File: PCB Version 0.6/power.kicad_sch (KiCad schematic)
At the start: 32 parts, among them IC5 LMR38025SDRRR, IC6 LMR38025SDRRR, U2 C5250982, U4 TPS2116DRL, U7 TPS746-3.3DRV

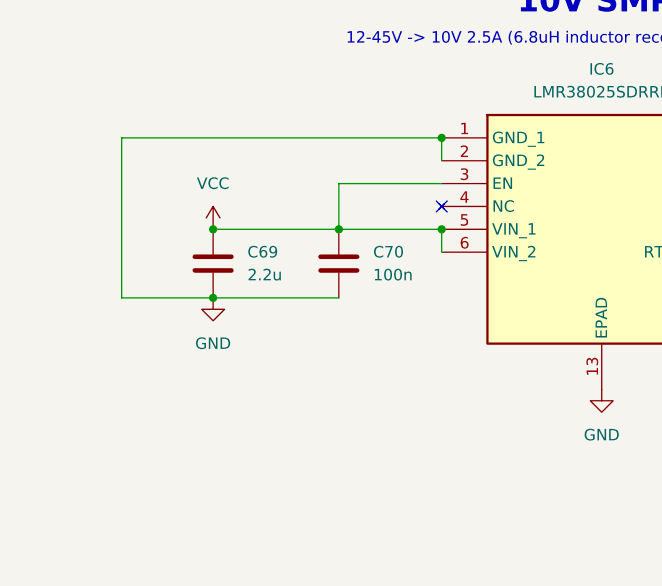
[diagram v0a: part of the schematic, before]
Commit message: remove current sensor ADC, swap opamp, add dcdc switch
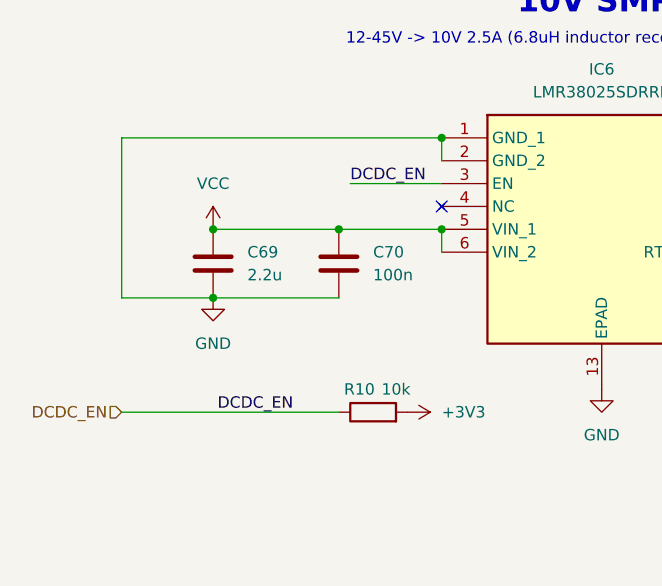
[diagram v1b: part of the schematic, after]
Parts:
- added R10: 10k, Resistor_SMD:R_0402_1005Metric, symbol Device:R
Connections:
- net VCC: no longer IC6.3 (EN)
- new net +3V3: R10.2
- new net DCDC_EN: IC6.3 (EN), R10.1
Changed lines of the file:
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@@
+	(wire
+		(pts
+			(xy 53.34 118.11) (xy 63.5 118.11)
+		)
+		(stroke
+			(width 0)
+			(type default)
+		)
+	)
 	(wire
 		(pts
@@
 	(wire
 		(pts
-			(xy 52.07 118.11) (xy 52.07 123.19)
-		)
-		(stroke
-			(width 0)
-			(type default)
-		)
-	)
-	(wire
-		(pts
 			(xy 265.43 123.19) (xy 265.43 121.92)
 		)
@@
 	(wire
 		(pts
+			(xy 27.94 143.51) (xy 52.07 143.51)
+		)
+		(stroke
+			(width 0)
+			(type default)
+		)
+	)
+	(wire
+		(pts
 			(xy 229.87 121.92) (xy 240.03 121.92)
 		)
@@
 	(wire
 		(pts
-			(xy 63.5 118.11) (xy 52.07 118.11)
-		)
-		(stroke
-			(width 0)
-			(type default)
-		)
-	)
-	(wire
-		(pts
 			(xy 109.22 113.03) (xy 113.03 113.03)
 		)
@@
 			(width 0)
 			(type default)
+		)
+	)
+	(label "DCDC_EN"
+		(at 53.34 118.11 0)
+		(effects
+			(font
+				(size 1.27 1.27)
+			)
+			(justify left bottom)
+		)
+	)
+	(label "DCDC_EN"
+		(at 46.99 143.51 180)
+		(effects
+			(font
+				(size 1.27 1.27)
+			)
+			(justify right bottom)
+		)
+	)
+	(hierarchical_label "DCDC_EN"
+		(shape input)
+		(at 27.94 143.51 180)
+		(effects
+			(font
+				(size 1.27 1.27)
+			)
+			(justify right)
 		)
 	)
@@
 	)
 	(symbol
+		(lib_id "Device:R")
+		(at 55.88 143.51 90)
+		(unit 1)
+		(exclude_from_sim no)
+		(in_bom yes)
+		(on_board yes)
+		(dnp no)
+		(property "Reference" "R10"
+			(at 54.356 140.97 90)
+			(effects
+				(font
+					(size 1.27 1.27)
+				)
+			)
+		)
+		(property "Value" "10k"
+			(at 58.42 140.97 90)
+			(effects
+				(font
+					(size 1.27 1.27)
+				)
+			)
+		)
+		(property "Footprint" "Resistor_SMD:R_0402_1005Metric"
+			(at 55.88 145.288 90)
+			(effects
+				(font
+					(size 1.27 1.27)
+				)
+				(hide yes)
+			)
+		)
+		(property "Datasheet" "~"
+			(at 55.88 143.51 0)
+			(effects
+				(font
+					(size 1.27 1.27)
+				)
+				(hide yes)
+			)
+		)
+		(property "Description" "Resistor"
+			(at 55.88 143.51 0)
+			(effects
+				(font
+					(size 1.27 1.27)
+				)
+				(hide yes)
+			)
+		)
+		(pin "2"
+		)
+		(pin "1"
+		)
+		(instances
+			(project ""
+				(path "/1651f454-30c0-48ea-9fcf-6c96a661786a/c47ad1ff-c88e-42df-ba75-e03e62e860dd"
+					(reference "R10")
+					(unit 1)
+				)
+			)
+		)
+	)
+	(symbol
 		(lib_id "power:GND")
 		(at 127 71.12 0)
@@
 					(unit 1)
 				)
+			)
+		)
+	)
+	(symbol
+		(lib_id "power:+3V3")
+		(at 59.69 143.51 270)
+		(unit 1)
+		(exclude_from_sim no)
+		(in_bom yes)
+		(on_board yes)
+		(dnp no)
+		(fields_autoplaced yes)
+		(property "Reference" "#PWR030"
+			(at 55.88 143.51 0)
+			(effects
+				(font
+					(size 1.27 1.27)
+				)
+				(hide yes)
+			)
+		)
+		(property "Value" "+3V3"
+			(at 63.5 143.5099 90)
+			(effects
+				(font
+					(size 1.27 1.27)
+				)
+				(justify left)
+			)
+		)
+		(property "Footprint" ""
+			(at 59.69 143.51 0)
+			(effects
+				(font
+					(size 1.27 1.27)
+				)
+				(hide yes)
+			)
+		)
+		(property "Datasheet" ""
+			(at 59.69 143.51 0)
+			(effects
+				(font
+					(size 1.27 1.27)
+				)
+				(hide yes)
+			)
+		)
+		(property "Description" "Power symbol creates a global label with name \"+3V3\""
+			(at 59.69 143.51 0)
+			(effects
+				(font
+					(size 1.27 1.27)
+				)
+				(hide yes)
+			)
+		)
+		(pin "1"
+		)
+		(instances
+			(project ""
+				(path "/1651f454-30c0-48ea-9fcf-6c96a661786a/c47ad1ff-c88e-42df-ba75-e03e62e860dd"
+					(reference "#PWR030")
+					(unit 1)
+				)

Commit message: Update power.kicad_sch
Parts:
- added C31: 10u, Capacitor_SMD:C_0402_1005Metric, symbol Device:C
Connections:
- net +3V3_ELRS: now also C31.1
- net GND: now also C31.2
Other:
- moved on the sheet: C83, C84, U7

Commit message: WIP layout
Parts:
- C65, C70, C71, C84: footprint Capacitor_SMD:C_0402_1005Metric_Pad0.74x0.62mm_HandSolder -> Capacitor_SMD:C_0402_1005Metric
- R13, R14, R15, R16, R17, R18, R19, R20: footprint Resistor_SMD:R_0402_1005Metric_Pad0.72x0.64mm_HandSolder -> Resistor_SMD:R_0402_1005Metric
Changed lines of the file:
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@@
 			)
 		)
-		(property "Footprint" "Resistor_SMD:R_0402_1005Metric_Pad0.72x0.64mm_HandSolder"
+		(property "Footprint" "Resistor_SMD:R_0402_1005Metric"
 			(at 186.182 63.5 90)
 			(effects
@@
 			)
 		)
-		(property "Footprint" "Resistor_SMD:R_0402_1005Metric_Pad0.72x0.64mm_HandSolder"
+		(property "Footprint" "Resistor_SMD:R_0402_1005Metric"
 			(at 114.3 72.898 90)
 			(effects
@@
 			)
 		)
-		(property "Footprint" "Resistor_SMD:R_0402_1005Metric_Pad0.72x0.64mm_HandSolder"
+		(property "Footprint" "Resistor_SMD:R_0402_1005Metric"
 			(at 114.3 135.128 90)
 			(effects
@@
 			)
 		)
-		(property "Footprint" "Resistor_SMD:R_0402_1005Metric_Pad0.72x0.64mm_HandSolder"
+		(property "Footprint" "Resistor_SMD:R_0402_1005Metric"
 			(at 125.222 118.11 90)
 			(effects
@@
 			)
 		)
-		(property "Footprint" "Resistor_SMD:R_0402_1005Metric_Pad0.72x0.64mm_HandSolder"
+		(property "Footprint" "Resistor_SMD:R_0402_1005Metric"
 			(at 125.222 128.27 90)
 			(effects
@@
 			)
 		)
-		(property "Footprint" "Capacitor_SMD:C_0402_1005Metric_Pad0.74x0.62mm_HandSolder"
+		(property "Footprint" "Capacitor_SMD:C_0402_1005Metric"
 			(at 108.2548 113.03 0)
 			(effects
@@
 			)
 		)
-		(property "Footprint" "Capacitor_SMD:C_0402_1005Metric_Pad0.74x0.62mm_HandSolder"
+		(property "Footprint" "Capacitor_SMD:C_0402_1005Metric"
 			(at 263.8552 130.81 0)
 			(effects
@@
 			)
 		)
-		(property "Footprint" "Capacitor_SMD:C_0402_1005Metric_Pad0.74x0.62mm_HandSolder"
+		(property "Footprint" "Capacitor_SMD:C_0402_1005Metric"
 			(at 108.2548 50.8 0)
 			(effects
@@
 			)
 		)
-		(property "Footprint" "Capacitor_SMD:C_0402_1005Metric_Pad0.74x0.62mm_HandSolder"
+		(property "Footprint" "Capacitor_SMD:C_0402_1005Metric"
 			(at 53.0352 130.81 0)
 			(effects
@@
 			)
 		)
-		(property "Footprint" "Resistor_SMD:R_0402_1005Metric_Pad0.72x0.64mm_HandSolder"
+		(property "Footprint" "Resistor_SMD:R_0402_1005Metric"
 			(at 125.222 66.04 90)
 			(effects
@@
 			)
 		)
-		(property "Footprint" "Resistor_SMD:R_0402_1005Metric_Pad0.72x0.64mm_HandSolder"
+		(property "Footprint" "Resistor_SMD:R_0402_1005Metric"
 			(at 125.222 55.88 90)
 			(effects
@@
 			)
 		)
-		(property "Footprint" "Resistor_SMD:R_0402_1005Metric_Pad0.72x0.64mm_HandSolder"
+		(property "Footprint" "Resistor_SMD:R_0402_1005Metric"
 			(at 186.182 71.12 90)
 			(effects

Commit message: wip layout
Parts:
- removed C82: 1u, Capacitor_SMD:C_0402_1005Metric, symbol Device:C
- C63, C64: footprint Capacitor_SMD:C_0603_1608Metric -> Capacitor_SMD:C_0402_1005Metric
- C68, C69: value 2.2u -> 4.7u; footprint Capacitor_SMD:C_1206_3216Metric -> Capacitor_SMD:C_0805_2012Metric
- U7: footprint Package_SON:WSON-6-1EP_2x2mm_P0.65mm_EP1x1.6mm_ThermalVias -> Package_SON:WSON-6-1EP_2x2mm_P0.65mm_EP1x1.6mm
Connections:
- net +3V3_ELRS is gone; now on net +3V3: C31.1, C84.1, U7.1 (OUT)
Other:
- moved on the sheet: C88
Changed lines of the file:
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@@
 	)
 	(junction
-		(at 195.58 128.27)
-		(diameter 0)
-		(color 0 0 0 0)
-	)
-	(junction
 		(at 274.32 121.92)
 		(diameter 0)
@@
 	)
 	(junction
-		(at 207.01 120.65)
-		(diameter 0)
-		(color 0 0 0 0)
-	)
-	(junction
 		(at 63.5 50.8)
 		(diameter 0)
@@
 	)
 	(junction
-		(at 195.58 120.65)
-		(diameter 0)
-		(color 0 0 0 0)
-	)
-	(junction
 		(at 109.22 113.03)
 		(diameter 0)
@@
 	)
 	(junction
+		(at 195.58 120.65)
+		(diameter 0)
+		(color 0 0 0 0)
+	)
+	(junction
 		(at 63.5 60.96)
 		(diameter 0)
@@
 	(wire
 		(pts
-			(xy 195.58 120.65) (xy 207.01 120.65)
-		)
-		(stroke
-			(width 0)
-			(type default)
-		)
-	)
-	(wire
-		(pts
 			(xy 99.06 50.8) (xy 109.22 50.8)
 		)
@@
 	(wire
 		(pts
-			(xy 195.58 128.27) (xy 207.01 128.27)
-		)
-		(stroke
-			(width 0)
-			(type default)
-		)
-	)
-	(wire
-		(pts
 			(xy 146.05 57.15) (xy 146.05 50.8)
 		)
@@
 			)
 		)
-		(property "Value" "2.2u"
+		(property "Value" "4.7u"
 			(at 41.91 128.2699 0)
 			(effects
@@
 			)
 		)
-		(property "Footprint" "Capacitor_SMD:C_1206_3216Metric"
+		(property "Footprint" "Capacitor_SMD:C_0805_2012Metric"
 			(at 39.0652 130.81 0)
 			(effects
@@
 			)
 		)
-		(property "Footprint" "Package_SON:WSON-6-1EP_2x2mm_P0.65mm_EP1x1.6mm_ThermalVias"
+		(property "Footprint" "Package_SON:WSON-6-1EP_2x2mm_P0.65mm_EP1x1.6mm"
 			(at 247.65 115.57 0)
 			(effects
@@
 			)
 		)
-		(property "Footprint" "Capacitor_SMD:C_0603_1608Metric"
+		(property "Footprint" "Capacitor_SMD:C_0402_1005Metric"
 			(at 245.4148 64.77 0)
 			(effects
@@
 	)
 	(symbol
-		(lib_id "Device:C")
-		(at 195.58 124.46 0)
-		(unit 1)
-		(exclude_from_sim no)
-		(in_bom yes)
-		(on_board yes)
-		(dnp no)
-		(fields_autoplaced yes)
-		(property "Reference" "C82"
-			(at 199.39 123.1899 0)
-			(effects
-				(font
-					(size 1.27 1.27)
-				)
-				(justify left)
-			)
-		)
-		(property "Value" "1u"
-			(at 199.39 125.7299 0)
-			(effects
-				(font
-					(size 1.27 1.27)
-				)
-				(justify left)
-			)
-		)
-		(property "Footprint" "Capacitor_SMD:C_0402_1005Metric"
-			(at 196.5452 128.27 0)
-			(effects
-				(font
-					(size 1.27 1.27)
-				)
-				(hide yes)
-			)
-		)
-		(property "Datasheet" "~"
-			(at 195.58 124.46 0)
-			(effects
-				(font
-					(size 1.27 1.27)
-				)
-				(hide yes)
-			)
-		)
-		(property "Description" "Unpolarized capacitor"
-			(at 195.58 124.46 0)
-			(effects
-				(font
-					(size 1.27 1.27)
-				)
-				(hide yes)
-			)
-		)
-		(pin "2"
-		)
-		(pin "1"
-		)
-		(instances
-			(project "Kolibri v0.6"
-				(path "/1651f454-30c0-48ea-9fcf-6c96a661786a/c47ad1ff-c88e-42df-ba75-e03e62e860dd"
-					(reference "C82")
-					(unit 1)
-				)
-			)
-		)
-	)
-	(symbol
 		(lib_id "Device:R")
 		(at 127 128.27 0)
@@
 			)
 		)
-		(property "Value" "2.2u"
+		(property "Value" "4.7u"
 			(at 41.91 66.0399 0)
 			(effects
@@
 			)
 		)
-		(property "Footprint" "Capacitor_SMD:C_1206_3216Metric"
+		(property "Footprint" "Capacitor_SMD:C_0805_2012Metric"
 			(at 39.0652 68.58 0)
 			(effects
@@
 	(symbol
 		(lib_id "power:+1V8")
-		(at 207.01 120.65 0)
+		(at 195.58 120.65 0)
 		(unit 1)
 		(exclude_from_sim no)
@@
 		(fields_autoplaced yes)
 		(property "Reference" "#PWR0143"
-			(at 207.01 124.46 0)
+			(at 195.58 124.46 0)
 			(effects
 				(font
@@
 		)
 		(property "Value" "+1V8"
-			(at 207.01 115.57 0)
+			(at 195.58 115.57 0)
 			(effects
 				(font
@@
 		)
 		(property "Footprint" ""
-			(at 207.01 120.65 0)
+			(at 195.58 120.65 0)
 			(effects
 				(font
@@
 		)
 		(property "Datasheet" ""
-			(at 207.01 120.65 0)
+			(at 195.58 120.65 0)
 			(effects
 				(font
@@
 		)
 		(property "Description" "Power symbol creates a global label with name \"+1V8\""
-			(at 207.01 120.65 0)
+			(at 195.58 120.65 0)
 			(effects
 				(font
@@
 			)
 		)
-		(property "Footprint" "Capacitor_SMD:C_0603_1608Metric"
+		(property "Footprint" "Capacitor_SMD:C_0402_1005Metric"
 			(at 258.1148 64.77 0)
 			(effects
@@
 			)
 		)
-		(property "Value" "+3V3_ELRS"
+		(property "Value" "+3V3"
 			(at 274.32 116.84 0)
 			(effects
@@
 	(symbol
 		(lib_id "Device:C")
-		(at 207.01 124.46 0)
+		(at 195.58 124.46 0)
 		(unit 1)
 		(exclude_from_sim no)
@@
 		(fields_autoplaced yes)
 		(property "Reference" "C88"
-			(at 210.82 123.1899 0)
+			(at 199.39 123.1899 0)
 			(effects
 				(font
@@
 		)
 		(property "Value" "10u"
-			(at 210.82 125.7299 0)
+			(at 199.39 125.7299 0)
 			(effects
 				(font
@@
 		)
 		(property "Footprint" "Capacitor_SMD:C_0402_1005Metric"
-			(at 207.9752 128.27 0)
+			(at 196.5452 128.27 0)
 			(effects
 				(font
@@
 		)
 		(property "Datasheet" "~"
-			(at 207.01 124.46 0)
+			(at 195.58 124.46 0)
 			(effects
 				(font
@@
 		)
 		(property "Description" "Unpolarized capacitor"
-			(at 207.01 124.46 0)
+			(at 195.58 124.46 0)
 			(effects
 				(font

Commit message: wip
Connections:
- net GND: now also C81.2, C88.2, U2.1 (GND)
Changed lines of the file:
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@@
+	)
+	(symbol
+		(lib_id "power:GND")
+		(at 182.88 128.27 0)
+		(unit 1)
+		(exclude_from_sim no)
+		(in_bom yes)
+		(on_board yes)
+		(dnp no)
+		(fields_autoplaced yes)
+		(property "Reference" "#PWR067"
+			(at 182.88 134.62 0)
+			(effects
+				(font
+					(size 1.27 1.27)
+				)
+				(hide yes)
+			)
+		)
+		(property "Value" "GND"
+			(at 182.88 133.35 0)
+			(effects
+				(font
+					(size 1.27 1.27)
+				)
+			)
+		)
+		(property "Footprint" ""
+			(at 182.88 128.27 0)
+			(effects
+				(font
+					(size 1.27 1.27)
+				)
+				(hide yes)
+			)
+		)
+		(property "Datasheet" ""
+			(at 182.88 128.27 0)
+			(effects
+				(font
+					(size 1.27 1.27)
+				)
+				(hide yes)
+			)
+		)
+		(property "Description" "Power symbol creates a global label with name \"GND\" , ground"
+			(at 182.88 128.27 0)
+			(effects
+				(font
+					(size 1.27 1.27)
+				)
+				(hide yes)
+			)
+		)
+		(pin "1"
+		)
+		(instances
+			(project "Kolibri v0.6"
+				(path "/1651f454-30c0-48ea-9fcf-6c96a661786a/c47ad1ff-c88e-42df-ba75-e03e62e860dd"
+					(reference "#PWR067")
+					(unit 1)
+				)
+			)
+		)
 	)
 	(symbol
